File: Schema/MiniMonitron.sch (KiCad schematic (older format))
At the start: 19 parts, among them J1 CONN_02X18, J2 CONN_01X06, J3 CONN_02X20, J4 RTC, U1 H11AA1M, U2 MCP2551-I/SN

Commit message: Modification du schema électrique, + ajout de fiche technique
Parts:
- removed J1: CONN_02X18, symbol CONN_02X18
- removed J3: CONN_02X20, symbol CONN_02X20
- removed J4: RTC, symbol CONN_02X03
- added B?: Battery_Holder_CR1220, symbol Battery_Holder_CR1220
- added C? (x3): 100nF, symbol C
- added J5: CONN_01X02, symbol CONN_01X02
- added J?: CONN_01X06, symbol CONN_01X06
- added J? (x2): CONN_02X20, symbol CONN_02X20
- added P1: conn2x18pcie, symbol conn2x18pcie
- added R?: 4.3k, symbol R
- added U?: PCF2129AT, symbol PCF2129AT
- added U?: AXB050X43-SRZ, symbol AXB050X43-SRZ
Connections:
- net labels added: 24VDC_pwr, 3V3_pwr, 5V_pwr, 7VDC_pwr, RS485_A, RS485_B, UART_RX, UART_TX, ZERO_CROSS
- net labels removed: 3.3Vpwr, RS485A, RS485B, Zero_cross
- wire segments 100 -> 71
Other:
- moved on the sheet: J2, R1, R2, R3, R4, R5, R6, R7, R8, S1, U1, U2

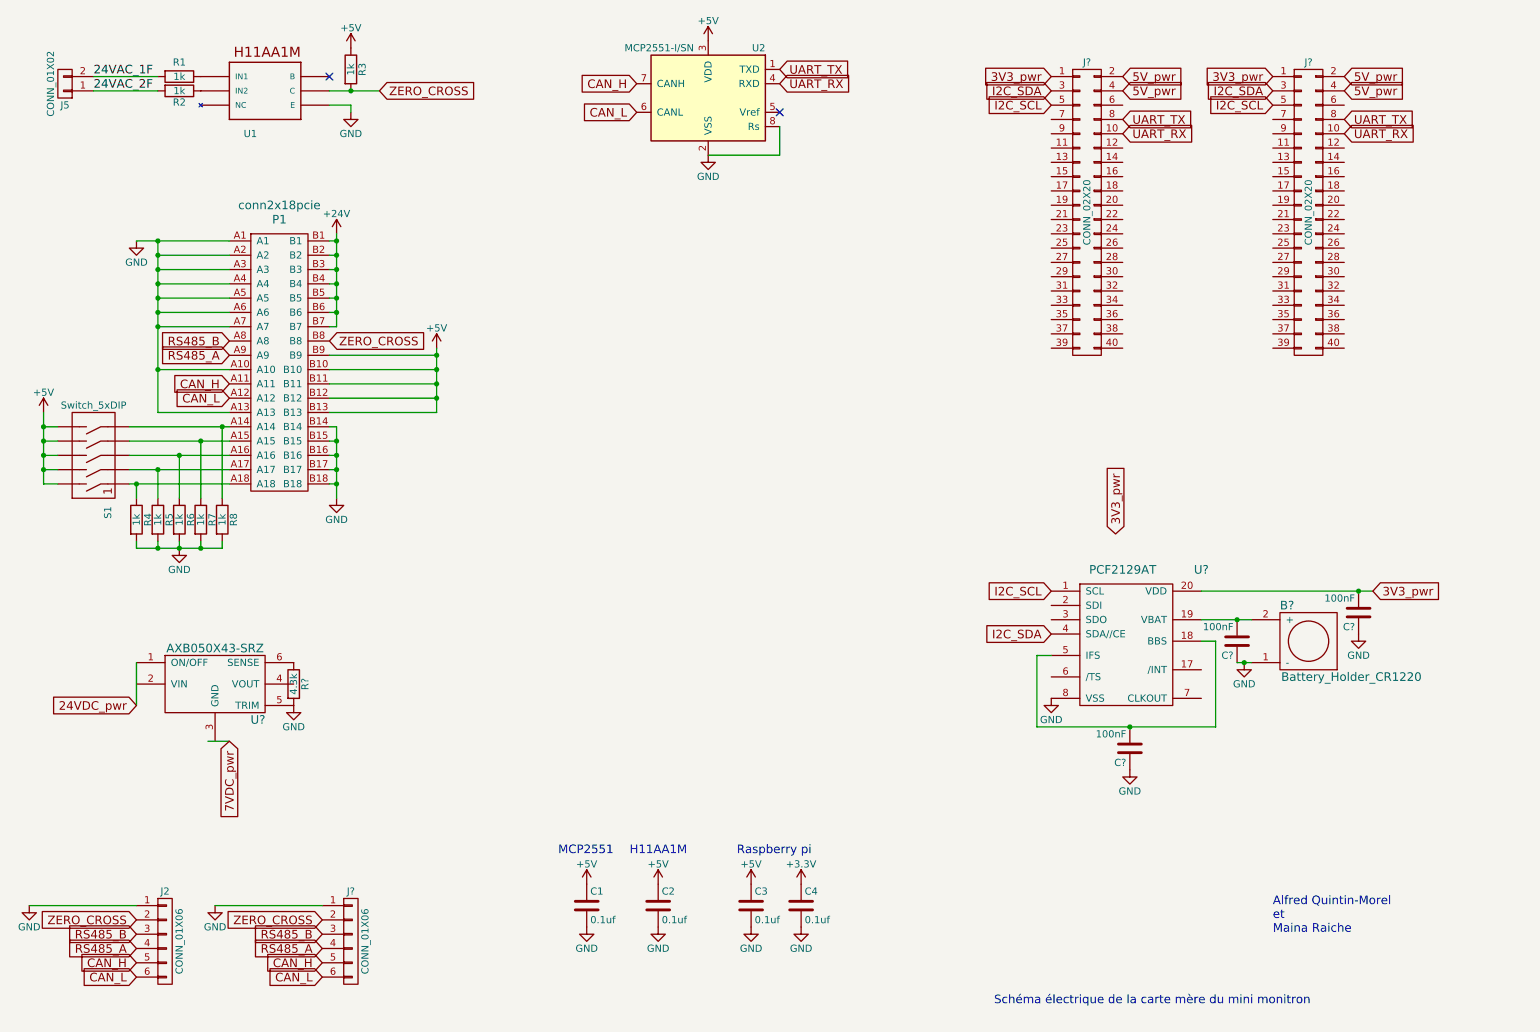
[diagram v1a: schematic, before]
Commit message: Ajout fiche technique + ajout alimentation sur schema electrique
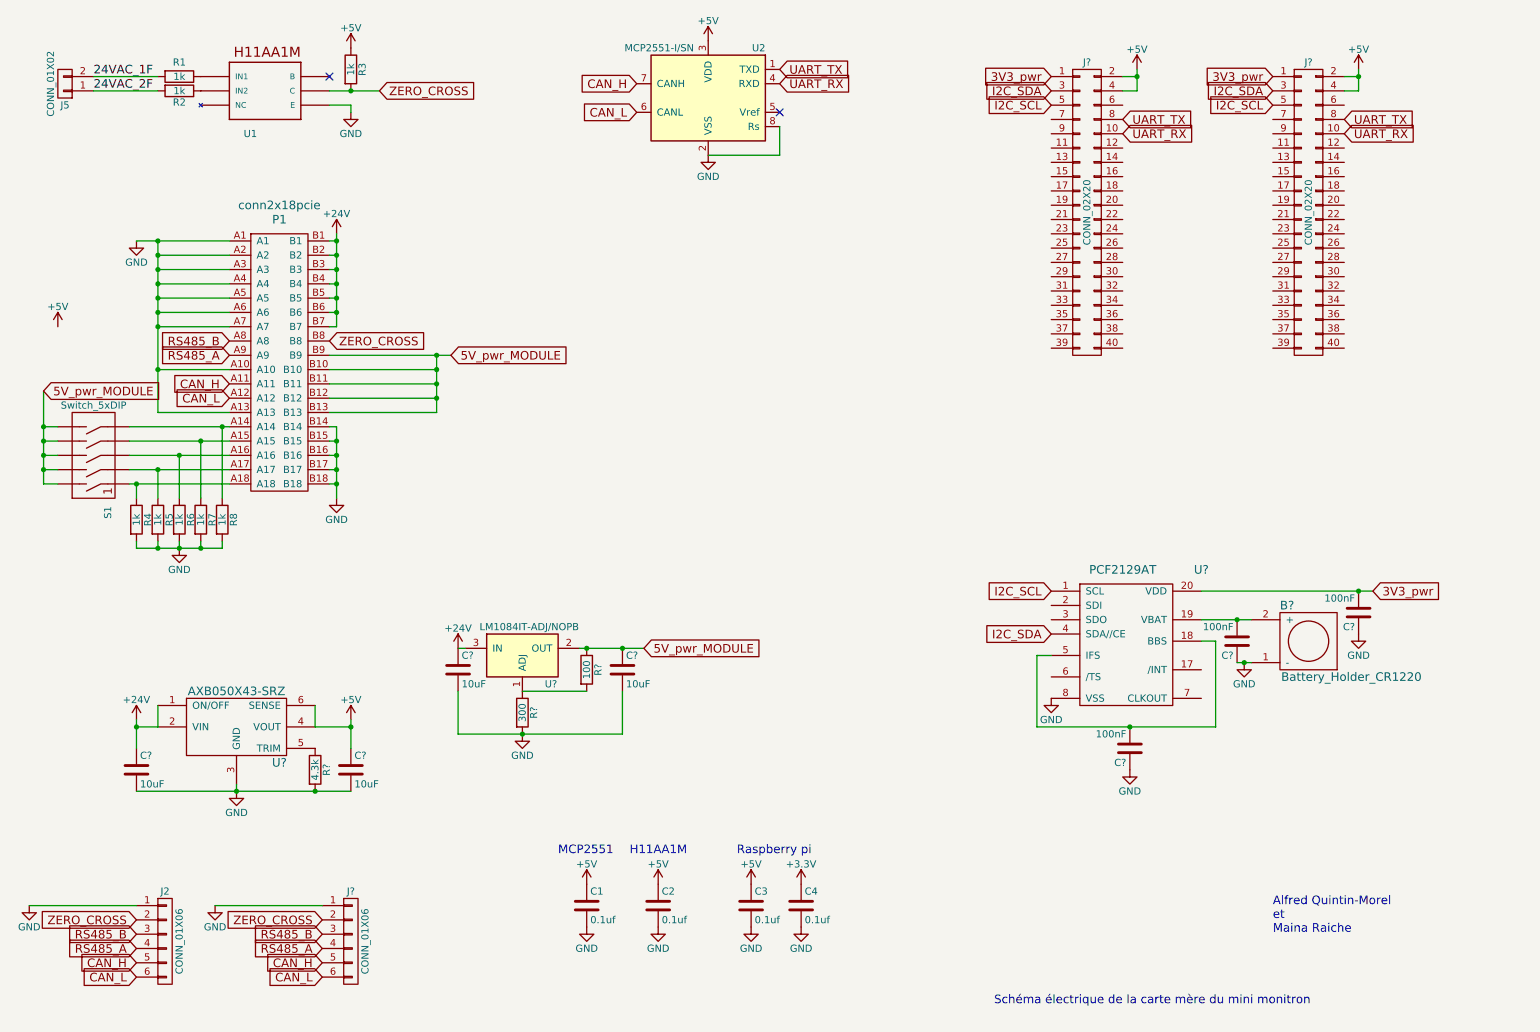
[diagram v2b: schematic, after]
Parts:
- added C? (x4): 10uF, symbol C
- added R?: 100, symbol R
- added R?: 300, symbol R
- added U?: LM1084IT-ADJ/NOPB, TO_SOT_Packages_THT:TO-220_Vertical, symbol LM1084IT-ADJ/NOPB
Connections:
- net 24VDC_pwr is gone; now on net +24V: U?.1 (ON/OFF)
- net 5V_pwr is gone; now on net +5V: J?.2 (P2), J?.2 (P2), J?.4 (P4), J?.4 (P4)
- net +24V: now also U?.2 (VIN), C?.1, C?.1, U?.3 (IN)
- net +5V: now also U?.4 (VOUT), U?.6 (SENSE), C?.1; no longer P1.B10, P1.B11, P1.B12, P1.B13, P1.B9, S1.10, S1.6, S1.7, S1.8, S1.9
- net GND: now also U?.3 (GND), C?.2, C?.2, C?.2, C?.2, R?.2; no longer U?.5 (TRIM)
- net at R?.1: now also U?.5 (TRIM); no longer U?.6 (SENSE)
- new net: R?.1, R?.2, U?.1 (ADJ)
- new net 5V_pwr_MODULE: C?.1, P1.B10, P1.B11, P1.B12, P1.B13, P1.B9, R?.1, S1.10, S1.6, S1.7, S1.8, S1.9, U?.2 (OUT)
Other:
- moved on the sheet: R?, U?

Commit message: ajout fiches technique + finalisation schema électrique + commencement PCB
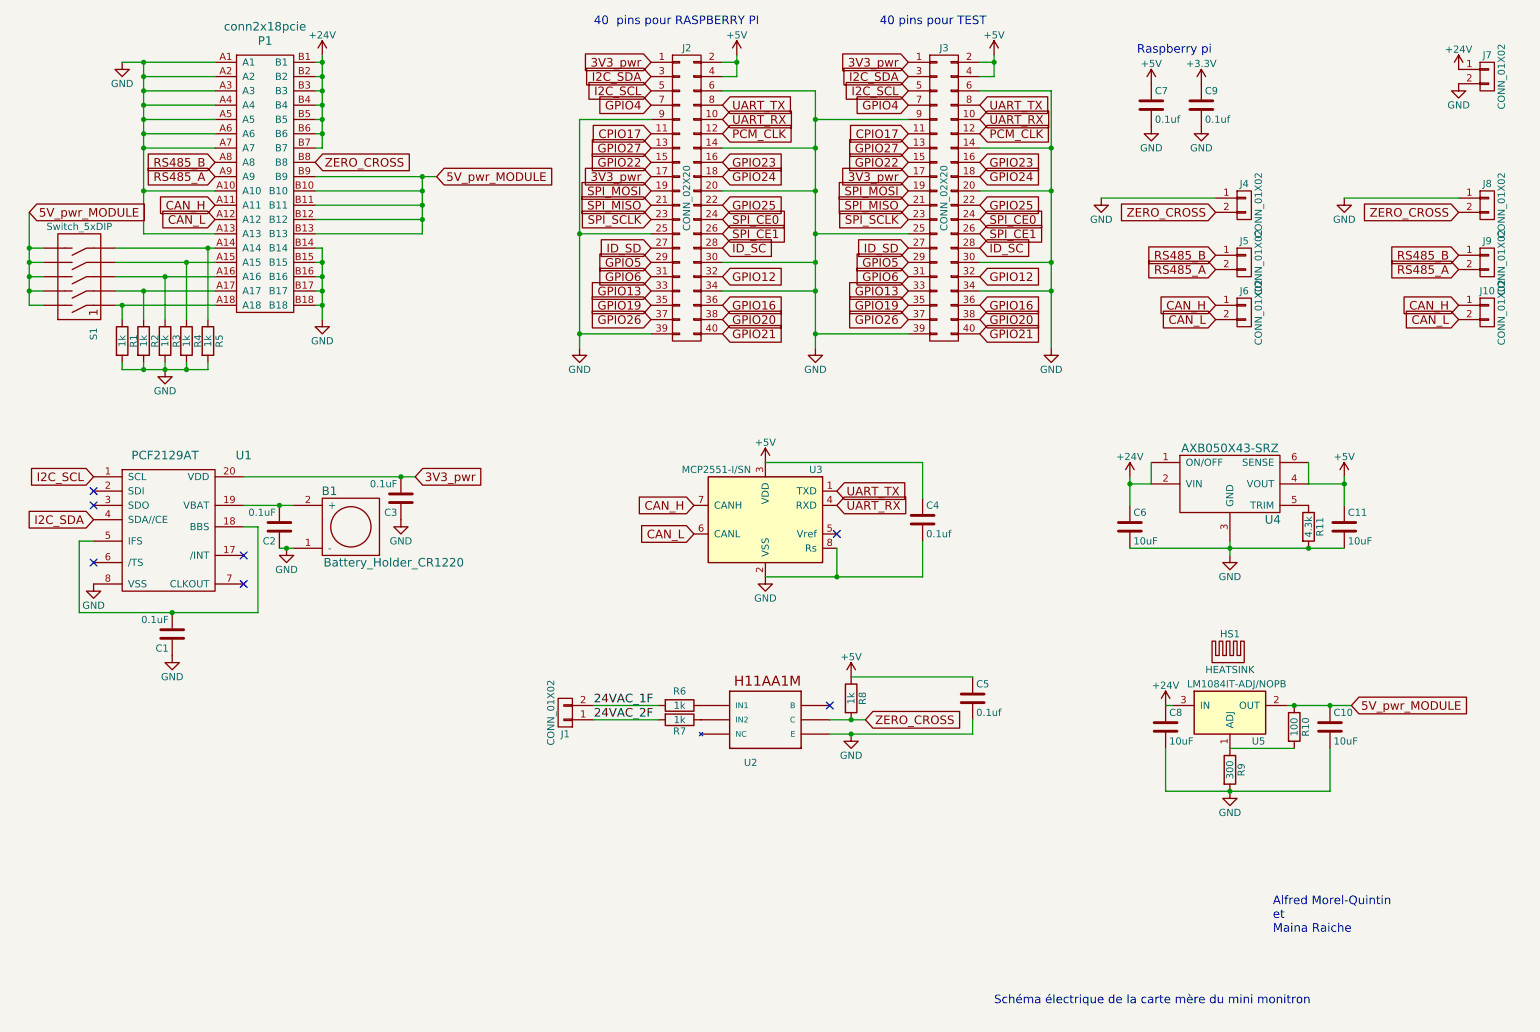
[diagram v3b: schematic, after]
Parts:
- removed J2, J?: CONN_01X06, symbol CONN_01X06
- added HS1: HEATSINK, mini_monitron:HeatSink_TO220_Vertical_1PP, symbol HEATSINK
- added J10, J4, J5, J6, J7, J8, J9: CONN_01X02, mini_monitron:bornier2, symbol CONN_01X02
- B1: renamed from B?; footprint (none) -> mini_monitron:keystone_1220
- C1, C2, C3: renamed from C?; value 100nF -> 0.1uF; footprint (none) -> mini_monitron:C_0805_HandSoldering
- C10, C11, C6, C8: renamed from C?; footprint (none) -> mini_monitron:C_0805_HandSoldering
- C4: renamed from C1; footprint (none) -> mini_monitron:C_0805_HandSoldering
- C5: renamed from C2; footprint (none) -> mini_monitron:C_0805_HandSoldering
- C7: renamed from C3; footprint (none) -> mini_monitron:C_0805_HandSoldering
- C9: renamed from C4; footprint (none) -> mini_monitron:C_0805_HandSoldering
- J1: renamed from J5; footprint (none) -> mini_monitron:bornier2
- J2: renamed from J?; footprint (none) -> mini_monitron:IDC_Header_Straight_40pins
- J3: renamed from J?; footprint (none) -> mini_monitron:Pin_Header_Straight_2x20_Pitch2.54mm
- P1: footprint (none) -> mini_monitron:pci-x_conn-x1_Vertical
- R1: renamed from R4; footprint (none) -> mini_monitron:R_0805_HandSoldering
- R10, R11, R9: renamed from R?; footprint (none) -> mini_monitron:R_0805_HandSoldering
- R2: renamed from R5; footprint (none) -> mini_monitron:R_0805_HandSoldering
- R3: renamed from R6; footprint (none) -> mini_monitron:R_0805_HandSoldering
- R4: renamed from R7; footprint (none) -> mini_monitron:R_0805_HandSoldering
- R5: renamed from R8; footprint (none) -> mini_monitron:R_0805_HandSoldering
- R6: renamed from R1; footprint (none) -> mini_monitron:R_0805_HandSoldering
- R7: renamed from R2; footprint (none) -> mini_monitron:R_0805_HandSoldering
- R8: renamed from R3; footprint (none) -> mini_monitron:R_0805_HandSoldering
- S1: footprint (none) -> mini_monitron:DIP-10_W7.62mm
- U1: renamed from U?; footprint (none) -> mini_monitron:SOIC-20W_7.5x12.8mm_Pitch1.27mm
- U2: renamed from U1; footprint DIP6 -> mini_monitron:DIP-6_W7.62mm
- U3: renamed from U2; footprint Housings_SOIC:SOIC-8_3.9x4.9mm_Pitch1.27mm -> mini_monitron:DIP-8_W7.62mm
- U4: renamed from U?; footprint (none) -> mini_monitron:AXB050X43-SRZ
- U5: renamed from U?; footprint TO_SOT_Packages_THT:TO-220_Vertical -> mini_monitron:TO-220_Horizontal
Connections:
- net +24V: now also J7.1 (P1)
- net 3V3_pwr: now also J2.17 (P17), J3.17 (P17)
- net CAN_H: now also J10.1 (P1), J6.1 (P1)
- net CAN_L: now also J10.2 (P2), J6.2 (P2)
- net GND: now also J2.14 (P14), J2.20 (P20), J2.25 (P25), J2.30 (P30), J2.34 (P34), J2.39 (P39), J2.6 (P6), J2.9 (P9), J3.14 (P14), J3.20 (P20), J3.25 (P25), J3.30 (P30), J3.34 (P34), J3.39 (P39), J3.6 (P6), J3.9 (P9), J4.1 (P1), J7.2 (P2), J8.1 (P1)
- net RS485_A: now also J5.2 (P2), J9.2 (P2)
- net RS485_B: now also J5.1 (P1), J9.1 (P1)
- net ZERO_CROSS: now also J4.2 (P2), J8.2 (P2)
- net CPIO17: now reaches J2.11 (P11)
- net CPIO17: now also J3.11 (P11)
- net PCM_CLK: now reaches J2.12 (P12)
- net PCM_CLK: now also J3.12 (P12)
- net GPIO27: now reaches J2.13 (P13)
- net GPIO27: now also J3.13 (P13)
- net GPIO22: now reaches J2.15 (P15)
- net GPIO22: now also J3.15 (P15)
- net GPIO23: now reaches J2.16 (P16)
- net GPIO23: now also J3.16 (P16)
- net GPIO24: now reaches J2.18 (P18)
- net GPIO24: now also J3.18 (P18)
- net SPI_MOSI: now reaches J2.19 (P19)
- net SPI_MOSI: now also J3.19 (P19)
- net SPI_MISO: now reaches J2.21 (P21)
- net SPI_MISO: now also J3.21 (P21)
- net GPIO25: now reaches J2.22 (P22)
- net GPIO25: now also J3.22 (P22)
- net SPI_SCLK: now reaches J2.23 (P23)
- net SPI_SCLK: now also J3.23 (P23)
- net SPI_CE0: now reaches J2.24 (P24)
- net SPI_CE0: now also J3.24 (P24)
- net SPI_CE1: now reaches J2.26 (P26)
- net SPI_CE1: now also J3.26 (P26)
- net ID_SD: now reaches J2.27 (P27)
- net ID_SD: now also J3.27 (P27)
- net ID_SC: now reaches J2.28 (P28)
- net ID_SC: now also J3.28 (P28)
- net GPIO5: now reaches J2.29 (P29)
- net GPIO5: now also J3.29 (P29)
- net GPIO6: now reaches J2.31 (P31)
- net GPIO6: now also J3.31 (P31)
- net GPIO12: now reaches J2.32 (P32)
- net GPIO12: now also J3.32 (P32)
- net GPIO13: now reaches J2.33 (P33)
- net GPIO13: now also J3.33 (P33)
- net GPIO19: now reaches J2.35 (P35)
- net GPIO19: now also J3.35 (P35)
- net GPIO16: now reaches J2.36 (P36)
- net GPIO16: now also J3.36 (P36)
- net GPIO26: now reaches J2.37 (P37)
- net GPIO26: now also J3.37 (P37)
- net GPIO20: now reaches J2.38 (P38)
- net GPIO20: now also J3.38 (P38)
- net GPIO21: now reaches J2.40 (P40)
- net GPIO21: now also J3.40 (P40)
- net GPIO4: now reaches J2.7 (P7)
- net GPIO4: now also J3.7 (P7)
- no-connect marks 2 -> 7
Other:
- note added: "40 pins pour RASPBERRY PI\n"
- note added: "40 pins pour TEST\n"
- note added: "Alfred Morel-Quintin\net\nMaina Raiche"
- note removed: "Alfred Quintin-Morel\net\nMaina Raiche"
- note removed: "H11AA1M"
- note removed: "MCP2551\n"
- moved on the sheet: B1, C1, C10, C11, C2, C3, C4, C5, C6, C7, C8, C9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
